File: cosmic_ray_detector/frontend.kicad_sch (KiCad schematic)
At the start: 14 parts

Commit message: add title block to schematics
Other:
- company: (none) -> University of Oxford
- title: (none) -> AITL Simple Cosmic Ray Detector
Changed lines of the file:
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@@
 (kicad_sch (version 20211123) (generator eeschema)
   (paper "A4")
+  (title_block
+    (title "AITL Simple Cosmic Ray Detector")
+    (company "University of Oxford")
+    (comment 1 "design by: Dan Weatherill")
+  )
   (junction (at 46.99 167.64) (diameter 0) (color 0 0 0 0)
   )

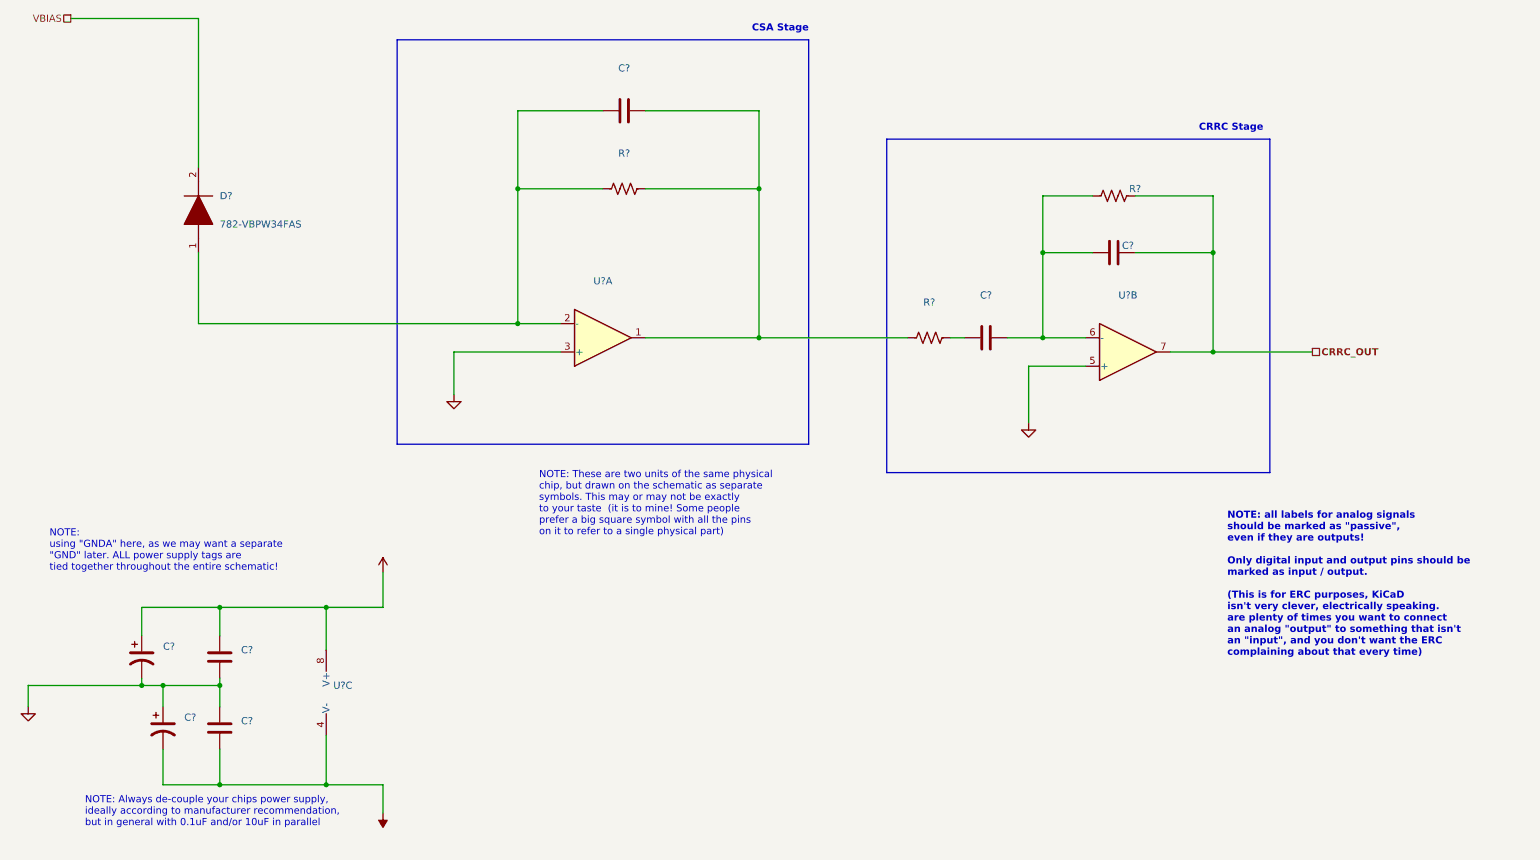
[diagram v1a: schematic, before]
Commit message: design of TLV3501 comparator sheet
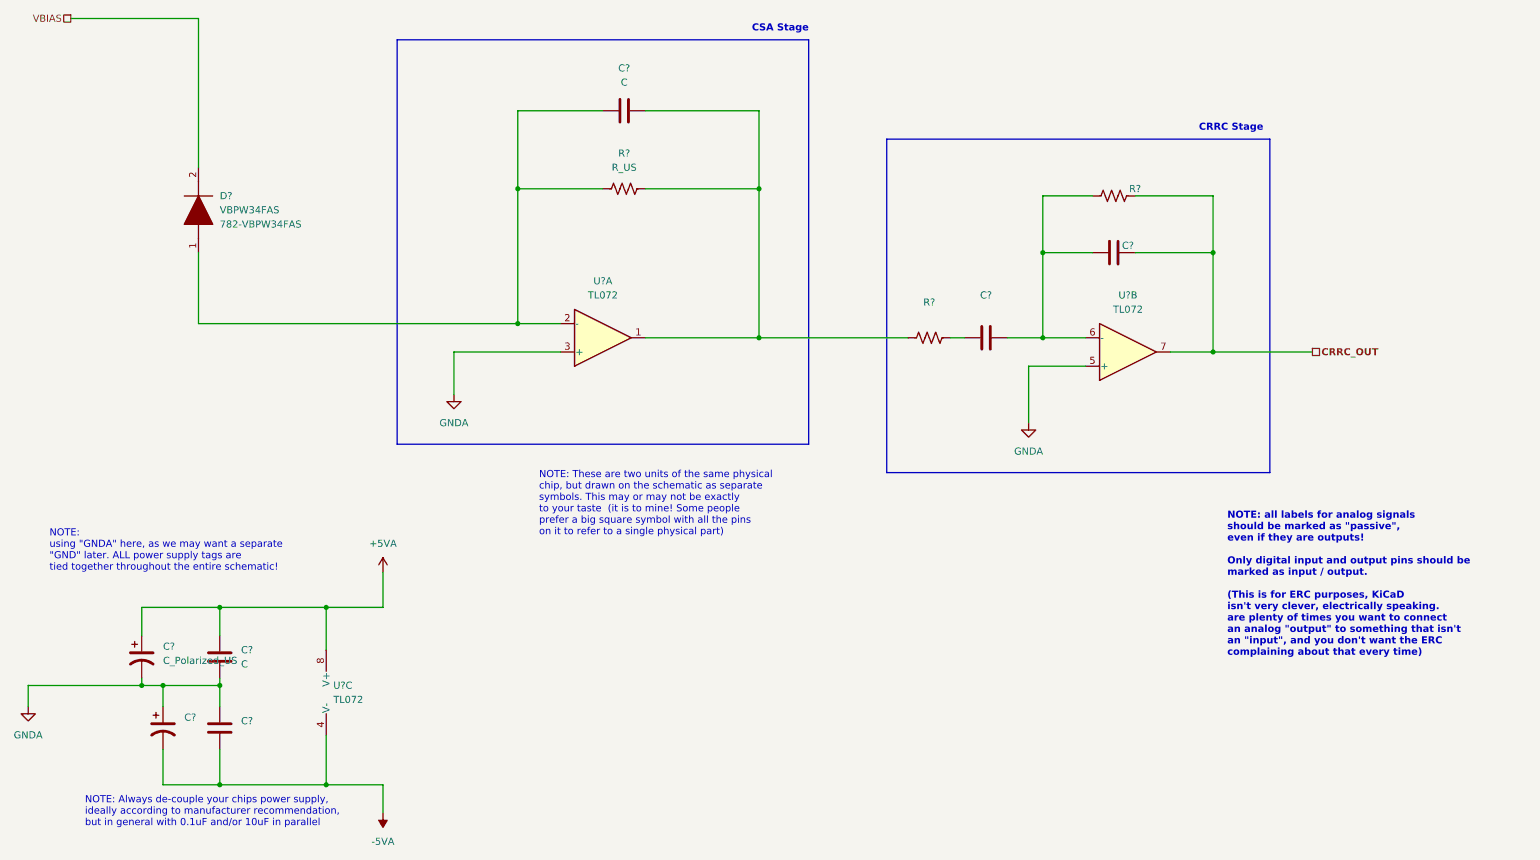
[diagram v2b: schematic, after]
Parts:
- C? (x2): value (none) -> C
- C?: value (none) -> C_Polarized_US
- D?: value (none) -> VBPW34FAS; footprint (none) -> VBPW34FAS
- R?: value (none) -> R_US
- U? (x3): value (none) -> TL072
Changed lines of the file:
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@@
       (effects (font (size 1.27 1.27)) hide)
     )
-    (property "Value" "" (id 1) (at 86.36 195.58 0))
+    (property "Value" "-5VA" (id 1) (at 86.36 195.58 0))
     (property "Footprint" "" (id 2) (at 86.36 190.5 0)
       (effects (font (size 1.27 1.27)) hide)
@@
     (in_bom yes) (on_board yes) (fields_autoplaced)
     (property "Reference" "U?" (id 0) (at 219.71 97.79 0))
-    (property "Value" "" (id 1) (at 219.71 100.33 0))
+    (property "Value" "TL072" (id 1) (at 219.71 100.33 0))
     (property "Footprint" "" (id 2) (at 219.71 107.95 0)
       (effects (font (size 1.27 1.27)) hide)
@@
     (in_bom yes) (on_board yes) (fields_autoplaced)
     (property "Reference" "R?" (id 0) (at 129.54 72.39 90))
-    (property "Value" "" (id 1) (at 129.54 74.93 90))
+    (property "Value" "R_US" (id 1) (at 129.54 74.93 90))
     (property "Footprint" "" (id 2) (at 129.794 77.724 90)
       (effects (font (size 1.27 1.27)) hide)
@@
       (effects (font (size 1.27 1.27)) hide)
     )
-    (property "Value" "" (id 1) (at 201.93 125.73 0))
+    (property "Value" "GNDA" (id 1) (at 201.93 125.73 0))
     (property "Footprint" "" (id 2) (at 201.93 120.65 0)
       (effects (font (size 1.27 1.27)) hide)
@@
       (effects (font (size 1.27 1.27)) (justify left))
     )
-    (property "Value" "" (id 1) (at 57.15 82.5499 90)
-      (effects (font (size 1.27 1.27)) (justify left))
-    )
-    (property "Footprint" "" (id 2) (at 53.34 86.36 0)
+    (property "Value" "VBPW34FAS" (id 1) (at 57.15 82.5499 90)
+      (effects (font (size 1.27 1.27)) (justify left))
+    )
+    (property "Footprint" "VBPW34FAS" (id 2) (at 53.34 86.36 0)
       (effects (font (size 1.27 1.27)) (justify left) hide)
     )
@@
       (effects (font (size 1.27 1.27)) (justify left))
     )
-    (property "Value" "" (id 1) (at 60.96 163.8299 0)
+    (property "Value" "C" (id 1) (at 60.96 163.8299 0)
       (effects (font (size 1.27 1.27)) (justify left))
     )
@@
       (effects (font (size 1.27 1.27)) hide)
     )
-    (property "Value" "" (id 1) (at 86.36 142.24 0))
+    (property "Value" "+5VA" (id 1) (at 86.36 142.24 0))
     (property "Footprint" "" (id 2) (at 86.36 147.32 0)
       (effects (font (size 1.27 1.27)) hide)
@@
       (effects (font (size 1.27 1.27)) (justify left))
     )
-    (property "Value" "" (id 1) (at 46.99 163.1949 0)
+    (property "Value" "C_Polarized_US" (id 1) (at 46.99 163.1949 0)
       (effects (font (size 1.27 1.27)) (justify left))
     )
@@
     (in_bom yes) (on_board yes) (fields_autoplaced)
     (property "Reference" "C?" (id 0) (at 129.54 57.15 90))
-    (property "Value" "" (id 1) (at 129.54 59.69 90))
+    (property "Value" "C" (id 1) (at 129.54 59.69 90))
     (property "Footprint" "" (id 2) (at 133.35 63.8048 0)
       (effects (font (size 1.27 1.27)) hide)
@@
       (effects (font (size 1.27 1.27)) hide)
     )
-    (property "Value" "" (id 1) (at 99.06 120.65 0))
+    (property "Value" "GNDA" (id 1) (at 99.06 120.65 0))
     (property "Footprint" "" (id 2) (at 99.06 115.57 0)
       (effects (font (size 1.27 1.27)) hide)
@@
       (effects (font (size 1.27 1.27)) hide)
     )
-    (property "Value" "" (id 1) (at 22.86 176.53 0))
+    (property "Value" "GNDA" (id 1) (at 22.86 176.53 0))
     (property "Footprint" "" (id 2) (at 22.86 171.45 0)
       (effects (font (size 1.27 1.27)) hide)
@@
     (in_bom yes) (on_board yes) (fields_autoplaced)
     (property "Reference" "U?" (id 0) (at 125.73 95.25 0))
-    (property "Value" "" (id 1) (at 125.73 97.79 0))
+    (property "Value" "TL072" (id 1) (at 125.73 97.79 0))
     (property "Footprint" "" (id 2) (at 125.73 105.41 0)
       (effects (font (size 1.27 1.27)) hide)
@@
       (effects (font (size 1.27 1.27)) (justify left))
     )
-    (property "Value" "" (id 1) (at 77.47 170.1799 0)
-      (effects (font (size 1.27 1.27)) (justify left))
-    )
+    (property "Value" "TL072" (id 1) (at 77.47 170.1799 0)
+      (effects (font (size 1.27 1.27)) (justify left))
+    )

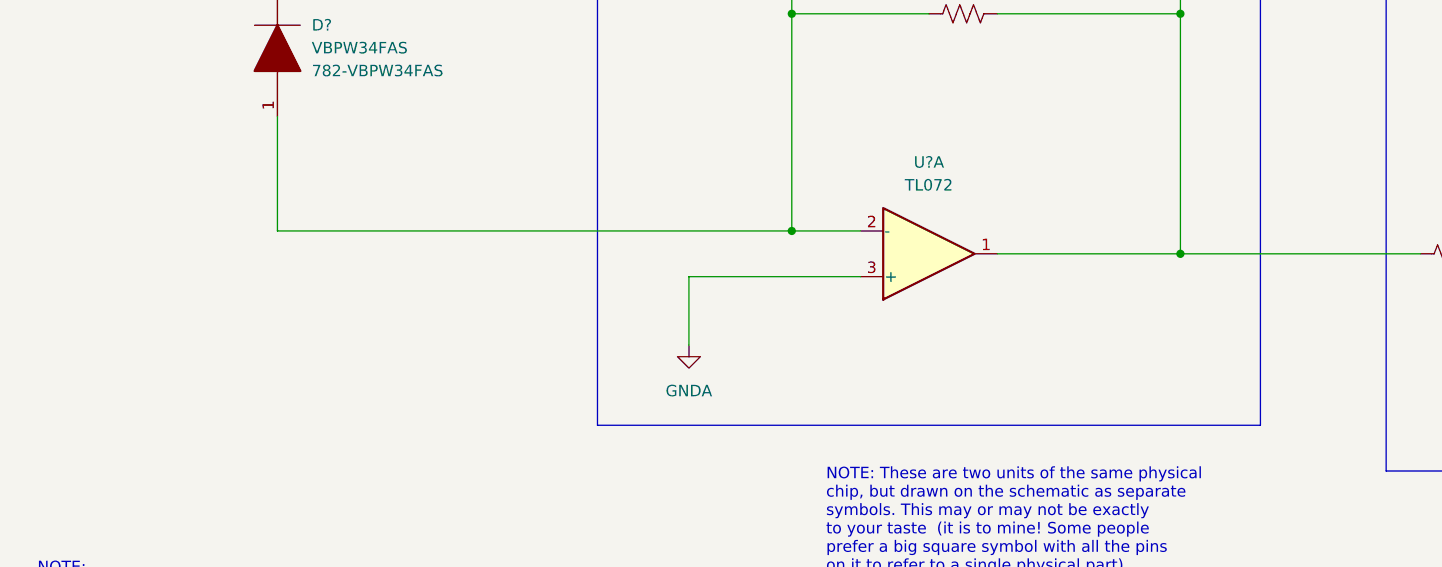
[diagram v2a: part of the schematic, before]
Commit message: add some net labels to frontends
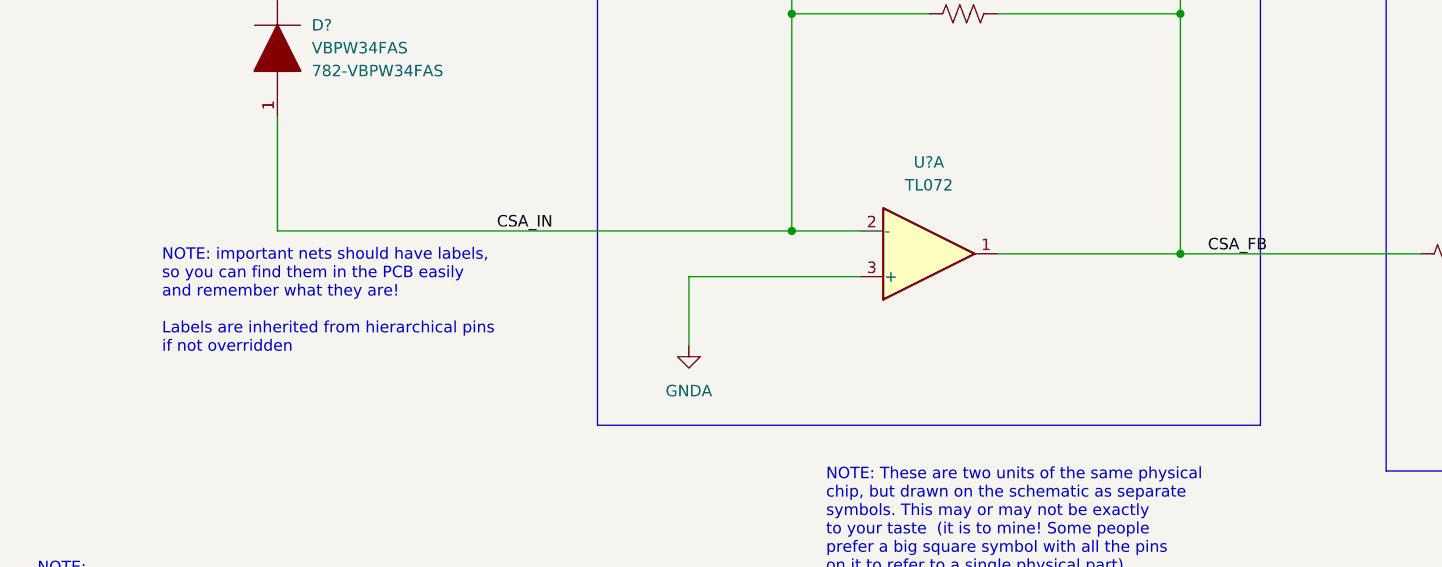
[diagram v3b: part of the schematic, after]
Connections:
- net CSA_IN: now reaches C?.1, D?.1, R?.1, U?.2 (-)
- net CSA_FB: now reaches C?.2, R?.1, R?.2, U?.1
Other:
- note added: "NOTE: important nets should have labels, so you can find them in the PCB easily and remember what they are! Labels are inherited from hierarchical pins if not overridden"
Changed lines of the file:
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@@
     (effects (font (size 1.27 1.27) bold) (justify left bottom))
+  )
+  (text "NOTE: important nets should have labels,\nso you can find them in the PCB easily\nand remember what they are!\n\nLabels are inherited from hierarchical pins\nif not overridden"
+    (at 40.513 116.586 0)
+    (effects (font (size 1.27 1.27)) (justify left bottom))
   )
   (text "NOTE: Always de-couple your chips power supply,\nideally according to manufacturer recommendation,\nbut in general with 0.1uF and/or 10uF in parallel\n"
@@
     (effects (font (size 1.27 1.27)) (justify left bottom))
   )
+  (label "CSA_IN" (at 77.724 102.87 0)
+    (effects (font (size 1.27 1.27)) (justify left bottom))
+  )
+  (label "CSA_FB" (at 156.718 105.41 0)
+    (effects (font (size 1.27 1.27)) (justify left bottom))
+  )
